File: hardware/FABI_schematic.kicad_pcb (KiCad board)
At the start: 2 copper layers, 81 x 55 mm, 74 parts, among them J1 Conn_01x02_Pin, J11 009159005551906, J11_GND1 Conn_01x01_Male, J11_VDD1 Conn_01x01_Male, J11_data1 Conn_01x01_Male, J12 Conn_01x04_Socket, J2 display_connector_91601-304LF, J3 54601-906WPLF, J4 54-00174 / FC68125, J5 54-00174 / FC68125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

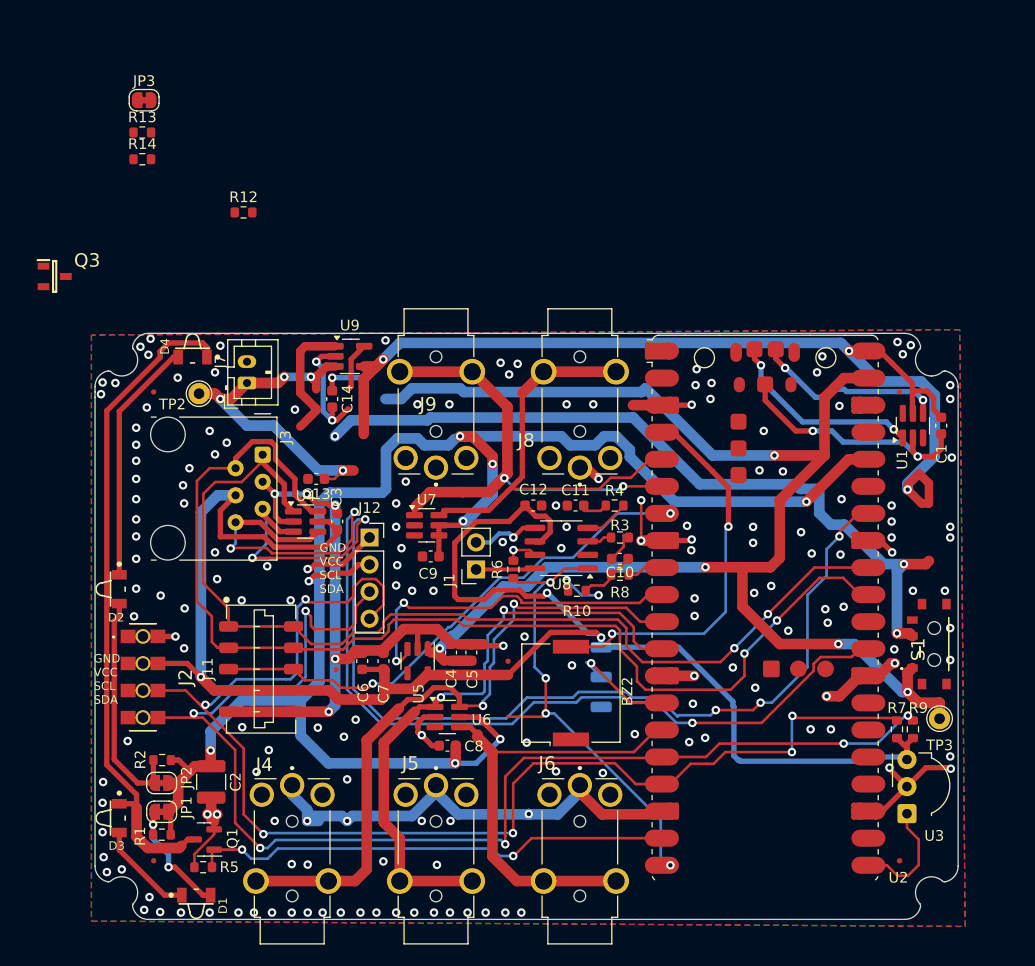
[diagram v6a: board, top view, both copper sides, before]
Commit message: Done more finetuning; No more ADC Pin on the Pico W left, waiting for response/recommendation of prof.; Made sure that every route is correct; Added new GPIO inputs, namely voltage divider so it would not constantly draw current (V_BATT_VD_SWITCH), (CHARGE_STAT) from the MCP STAT pin;
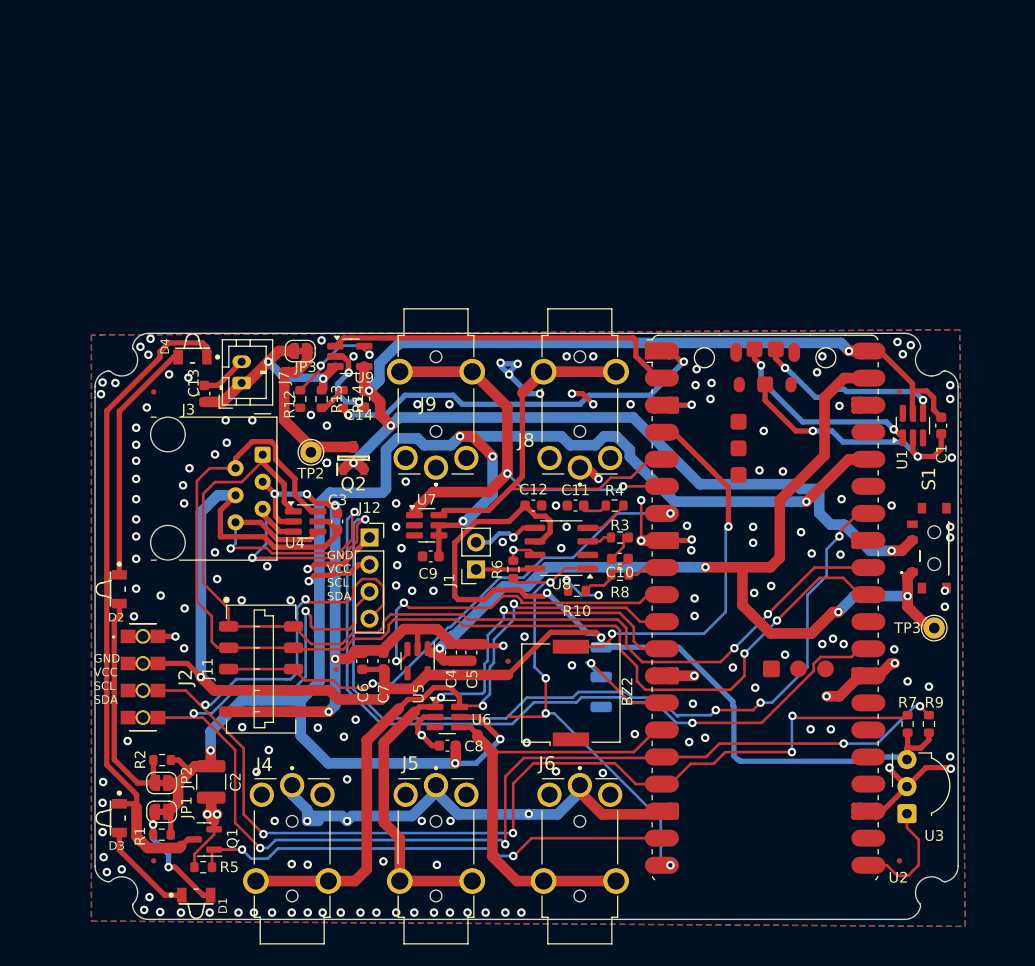
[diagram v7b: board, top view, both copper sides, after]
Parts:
- removed Q3: DMG2305UXQ-7, p-MOS:SOT96P240X110-3N
- added Q2: DMG2305UXQ-7, p-MOS:SOT96P240X110-3N, F.Cu at (111.5, 95.5)
- moved R13 30.1 mm to (108.5, 90.0), turned to -90 degrees
- moved R14 29.3 mm to (110.5, 90.0), turned to -90 degrees
- moved JP3 27.7 mm to (106.5, 85.5), turned to 180 degrees
- moved R12 18.3 mm to (106.5, 90.0), turned to -90 degrees
- moved C13 13.2 mm to (97.5, 89.5), turned to 90 degrees
- moved TP2 11.9 mm to (107.5, 95.0)
- moved S1 9.00 mm to (166.0, 104.0)
- moved TP3 8.51 mm to (166.0, 111.5)
- moved C14 3.00 mm to (112.5, 90.0)
- moved R9 1.58 mm to (165.5, 120.5)
- moved R7 1.12 mm to (163.5, 120.5)
- moved J7 0.50 mm to (101.0, 88.5)
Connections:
- R14 pad 2: /LPW1/V_BATT_PIN -> V_BATT_VD_SWITCH
- U2 pad 1: /V_BATT_PIN -> V_BATT_VD_SWITCH
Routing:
- net VSYS: track 135.7 -> 89.7 mm, vias 5 -> 4
- net V_PWR_SWITCH: track 174.8 -> 133.0 mm, vias 7 -> 5
- net V_BATT_VD_SWITCH: track 0.00 -> 36.8 mm, vias 0 -> 2
- net CHARGE_STAT: track 11.8 -> 34.2 mm
- net Net-(JP3-A): track 0.00 -> 16.3 mm
- net V_BATT: track 32.9 -> 18.9 mm, vias 4 -> 2
- net GND: track 193.5 -> 200.0 mm, vias 184 -> 189
- net Net-(U9-PROG): track 4.66 -> 9.81 mm, vias 0 -> 2
- net V_BATT_MEASURE: track 0.00 -> 2.68 mm
- net /SDA_INT: track 121.7 -> 123.7 mm
- net +3.3VADC: track 167.4 -> 169.5 mm
- net /SCL_INT: track 124.5 -> 125.5 mm
- net VCC: track 159.3 -> 159.9 mm

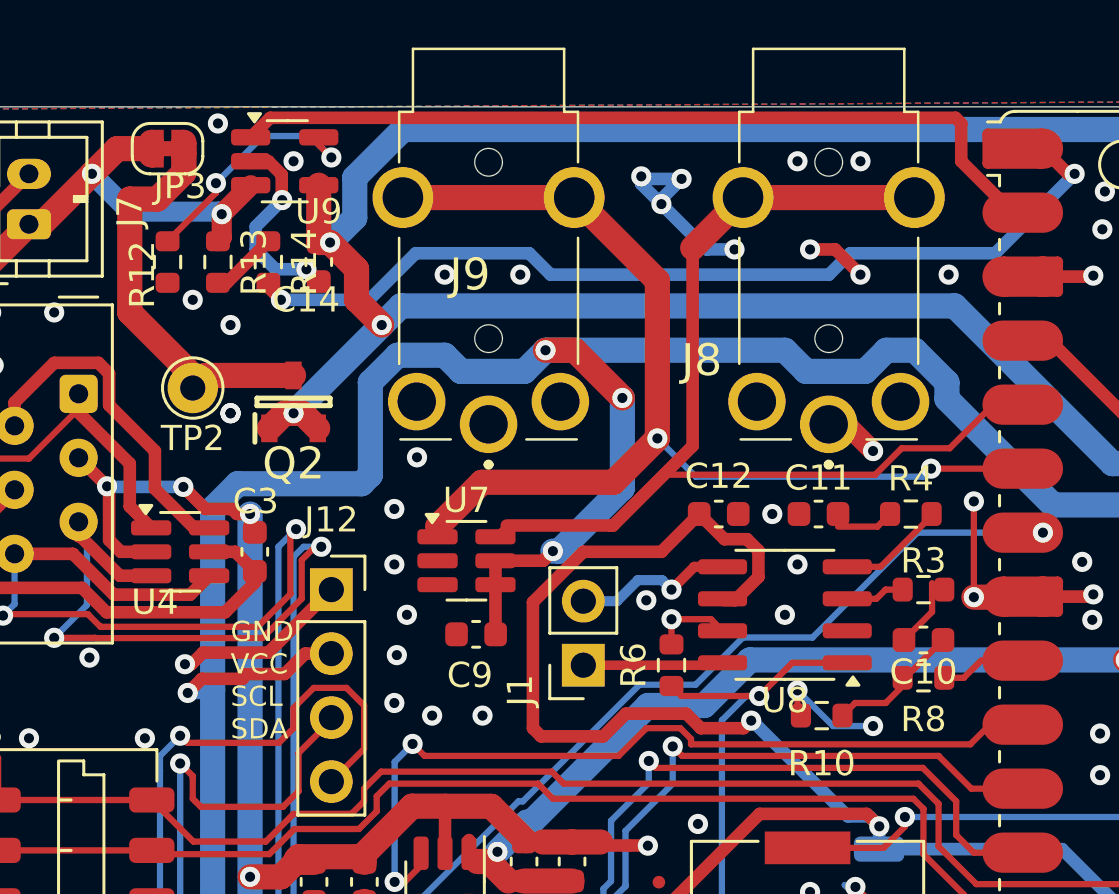
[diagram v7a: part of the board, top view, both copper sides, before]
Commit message: Checked for correct wiring of new conductor tracks (new, in the scope of this project); Layout improved;
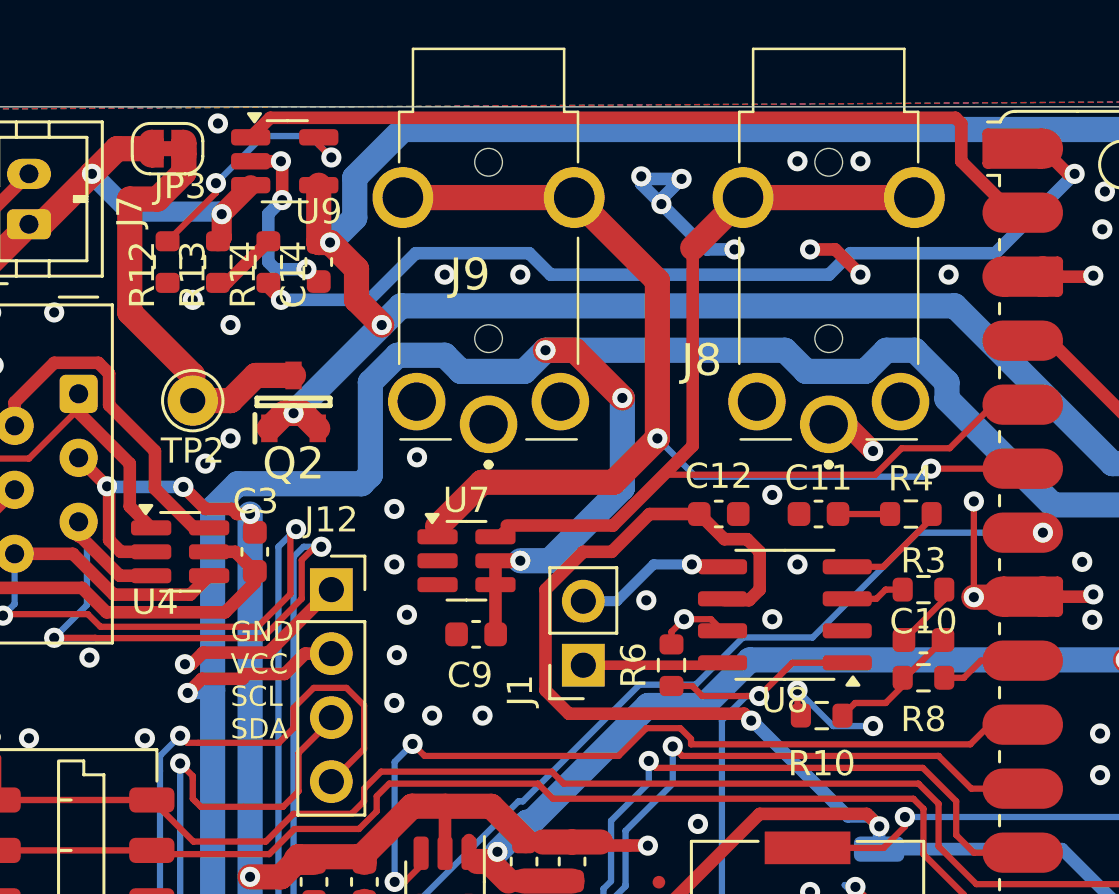
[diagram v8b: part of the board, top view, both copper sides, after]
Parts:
- moved TP2 0.50 mm to (107.5, 95.5)
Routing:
- net +3.3VADC: track 169.5 -> 167.2 mm
- net Net-(JP3-A): track 16.3 -> 17.0 mm
